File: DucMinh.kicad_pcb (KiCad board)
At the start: 2 copper layers, 80 x 70 mm, 51 parts, among them J5 USB_B_Micro, J8 Conn_01x04, U1 STM32F103C8T6, U2 AMS1117-3.3, U3 LM2596SX-5.0/NOPB, U4 TMC2209_SILENTSTEPSTICK, Y1 8 MHz, Y3 32.768 kHz

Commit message: fix routes
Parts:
- C11: value 10uF -> 10uf; footprint Capacitor_SMD:C_1206_3216Metric_Pad1.33x1.80mm_HandSolder -> ul_tantalum6032:tue_tantalum_6032
- R2: footprint Capacitor_SMD:C_0603_1608Metric_Pad1.08x0.95mm_HandSolder -> Resistor_SMD:R_0603_1608Metric_Pad0.98x0.95mm_HandSolder
- moved C11 6.54 mm to (102.1, 104.3), turned to 0 degrees
- moved R11 5.80 mm to (113.0, 94.8)
- moved R14 5.80 mm to (113.0, 93.2)
- moved R15 5.80 mm to (113.0, 91.5)
- moved PWR1 5.13 mm to (96.5, 110.1)
- moved R3 5.13 mm to (96.5, 113.6), turned to 0 degrees
- moved U2 3.46 mm to (96.5, 104.8)
- moved C19 1.87 mm to (109.1, 96.7)
- moved R2 1.75 mm to (96.5, 111.9)
- renumbered PWR to PWR1, SW to SW1, TMC_EN to TMC_EN1
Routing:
- net VIN_LDO: track 12.7 -> 0.00 mm
- net +3V3: track 224.5 -> 234.5 mm
- net USB-: track 10.4 -> 15.6 mm
- net USB+: track 11.2 -> 15.8 mm
- net GND: track 43.5 -> 39.1 mm, vias 42 -> 44
- net RESET: track 45.7 -> 47.9 mm
- net Net-(J5-D+): track 16.4 -> 14.4 mm
- net Net-(J5-D-): track 16.5 -> 14.9 mm

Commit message: .
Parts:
- removed BOOT1: BOOT1, ul_switch-SS12D00:tue_SS12D00_3P_2.5mm
- removed C15, C16: 10pf, Capacitor_SMD:C_0603_1608Metric_Pad1.08x0.95mm_HandSolder
- removed Y3: 32.768 kHz, ul_crytsal_mc306:SOJ_MC-306_EPS
- added STLink_EN: POWER, Connector_PinHeader_2.54mm:PinHeader_1x02_P2.54mm_Vertical, F.Cu at (125.7, 117.9)
- SWD1: value SWD -> Conn_01x04; footprint Connector_PinHeader_2.54mm:PinHeader_1x03_P2.54mm_Vertical -> Connector_JST:JST_XH_B4B-XH-A_1x04_P2.50mm_Vertical
- moved R7 12.7 mm to (117.8, 105.7), turned to -45 degrees
- moved C14 9.78 mm to (140.3, 122.7), turned to 0 degrees
- moved R8 9.04 mm to (112.2, 125.1), turned to 180 degrees
- moved BOOT0 7.03 mm to (110.0, 129.4)
- moved Y1 5.70 mm to (136.1, 126.4)
- moved SWD1 5.38 mm to (125.7, 126.8)
- moved R4 3.43 mm to (130.9, 110.9), turned to 135 degrees
- moved R5 2.17 mm to (134.9, 89.5)
- moved TMC_EN 2.17 mm to (133.0, 89.4)
- moved PC13 1.98 mm to (130.0, 114.0)
- moved C13 0.81 mm to (136.9, 122.7), turned to 180 degrees
- moved C7 0.81 mm to (134.9, 108.7)
- moved FB1 0.81 mm to (138.5, 108.5)
- moved C8 0.81 mm to (136.1, 109.8)
- moved C6 0.76 mm to (133.7, 107.5)
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- renumbered PWR1 to PWR, TMC_EN1 to TMC_EN
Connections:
- PWM1 pad 1-3: unconnected-(PWM1-Pad1-3) -> 5V_Drive
- PWM1 pad 2-3: unconnected-(PWM1-Pad2-3) -> 5V_Drive
- PWM1 pad 3-3: unconnected-(PWM1-Pad3-3) -> 5V_Drive
- R7 pad 1: BOOT1 -> GND
- SWD1 pad 1: GND -> 3V3_STLINK
- U1 pad 3: LSE_OCS_IN -> unconnected-(U1A-PC14-OSC32_IN-Pad3)
- U1 pad 4: LSE_OCS_OUT -> unconnected-(U1A-PC15-OSC32_OUT-Pad4)
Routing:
- net +3V3: track 234.5 -> 156.7 mm, vias 6 -> 4
- net LSE_OCS_OUT: track 22.9 -> 0.00 mm
- net LSE_OCS_IN: track 15.0 -> 0.00 mm
- net Net-(U1A-PB2): track 26.2 -> 13.3 mm
- net GND: track 39.1 -> 27.3 mm, vias 44 -> 46
- net SWD_CLK: track 17.2 -> 27.3 mm
- net Net-(U1A-BOOT0): track 15.2 -> 22.9 mm, vias 2 -> 4
- net HSE_OCS_OUT: track 31.0 -> 23.3 mm
- net SWD_IO: track 23.7 -> 31.2 mm
- net BOOT1: track 7.03 -> 0.00 mm
- net 3V3_STLINK: track 0.00 -> 6.31 mm
- net 5V_Drive: track 0.00 -> 5.08 mm
- net BOOT0: track 7.02 -> 3.17 mm
- net PC13_LED: track 5.61 -> 2.24 mm
- net HSE_OCS_IN: track 21.1 -> 22.4 mm
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- added copper zone on F.Cu, net (none)
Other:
- board text added: "5V"
- board text added: "CLK"
- board text added: "Default: Jumper OFF"
- board text added: "IO"
- board text removed: "SWD"
- board text removed: "clk"
- board text removed: "gnd"
- board text removed: "io"

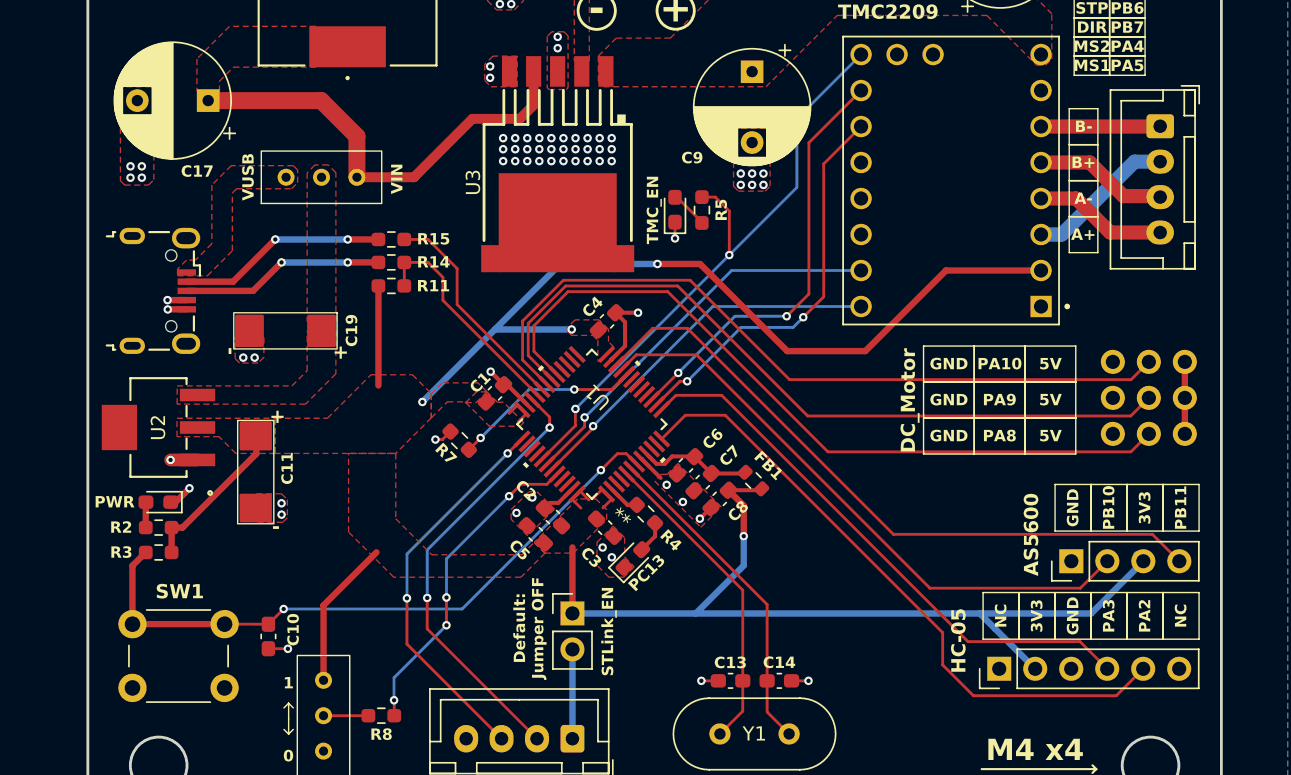
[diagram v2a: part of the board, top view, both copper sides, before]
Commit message: add 74hct125 routes
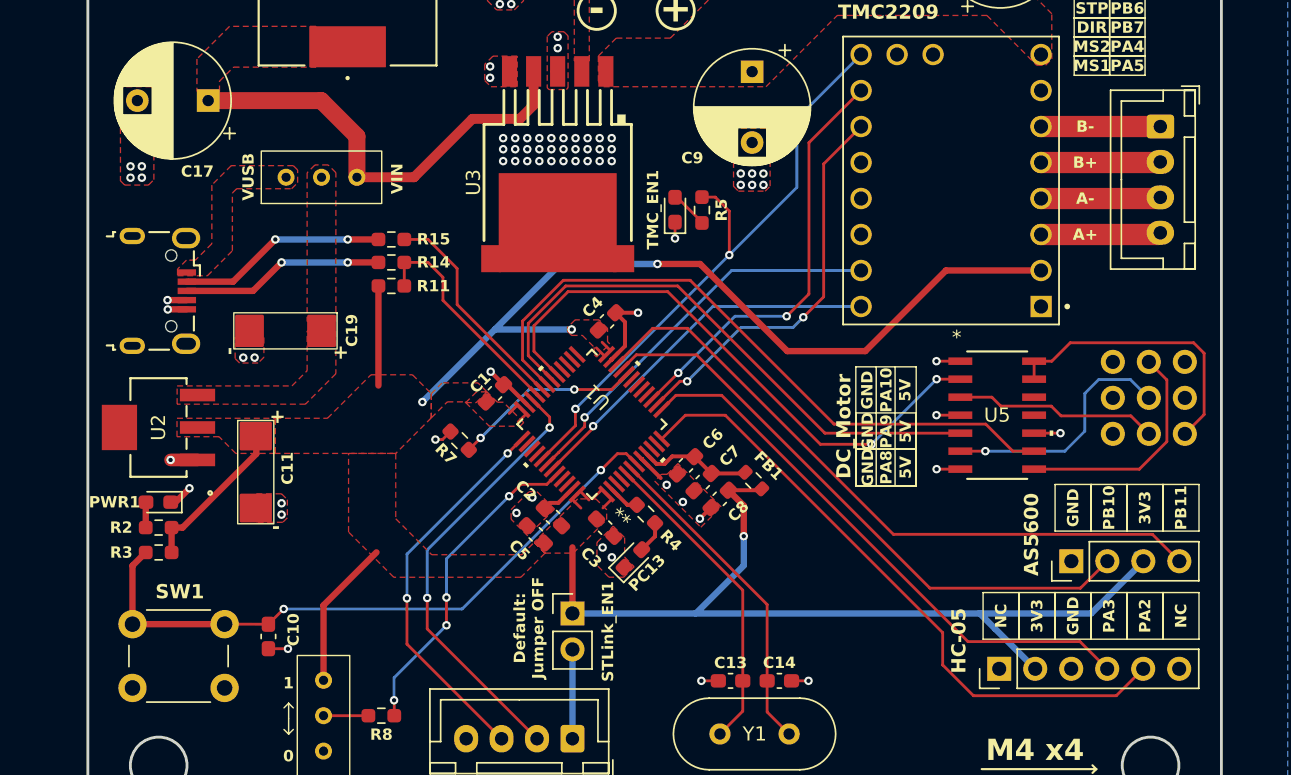
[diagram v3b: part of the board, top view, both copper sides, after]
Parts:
- added U5: 74HCT125D, tue_74hct125:SOT108-1_NXP, F.Cu at (155.7, 103.9)
- C18: value 100nf -> 470uf
- renumbered PWR to PWR1, STLink_EN to STLink_EN1, TMC_EN to TMC_EN1
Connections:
- J8 pad 2: Motor_B+ -> Motor_A-
- J8 pad 3: Motor_A- -> Motor_A+
- J8 pad 4: Motor_A+ -> Motor_B+
- PWM1 pad 1-2: PWM1 -> PWM1_out
- PWM1 pad 1-3: 5V_Drive -> 5V_Drive1
- PWM1 pad 2-2: PWM2 -> PWM2_out
- PWM1 pad 2-3: 5V_Drive -> 5V_Drive2
- PWM1 pad 3-2: PWM3 -> PWM3_out
- PWM1 pad 3-3: 5V_Drive -> 5V_Drive3
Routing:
- net 5V_Drive1: track 0.00 -> 20.4 mm
- net PWM2_out: track 0.00 -> 17.5 mm, vias 0 -> 1
- net PWM3_out: track 0.00 -> 16.3 mm
- net PWM1_out: track 0.00 -> 14.4 mm
- net PWM2: track 54.0 -> 40.6 mm
- net PWM1: track 53.7 -> 41.6 mm, vias 0 -> 2
- net GND: track 27.3 -> 34.2 mm, vias 46 -> 50
- net PWM3: track 54.0 -> 47.5 mm
- net 5V_Drive: track 5.08 -> 0.00 mm
- net Motor_B+: track 10.5 -> 8.47 mm
- net +3V3: track 156.7 -> 158.3 mm
- net Motor_A-: track 9.42 -> 8.44 mm
- net Motor_A+: track 9.40 -> 8.51 mm
- removed copper zone on F.Cu, net (none)

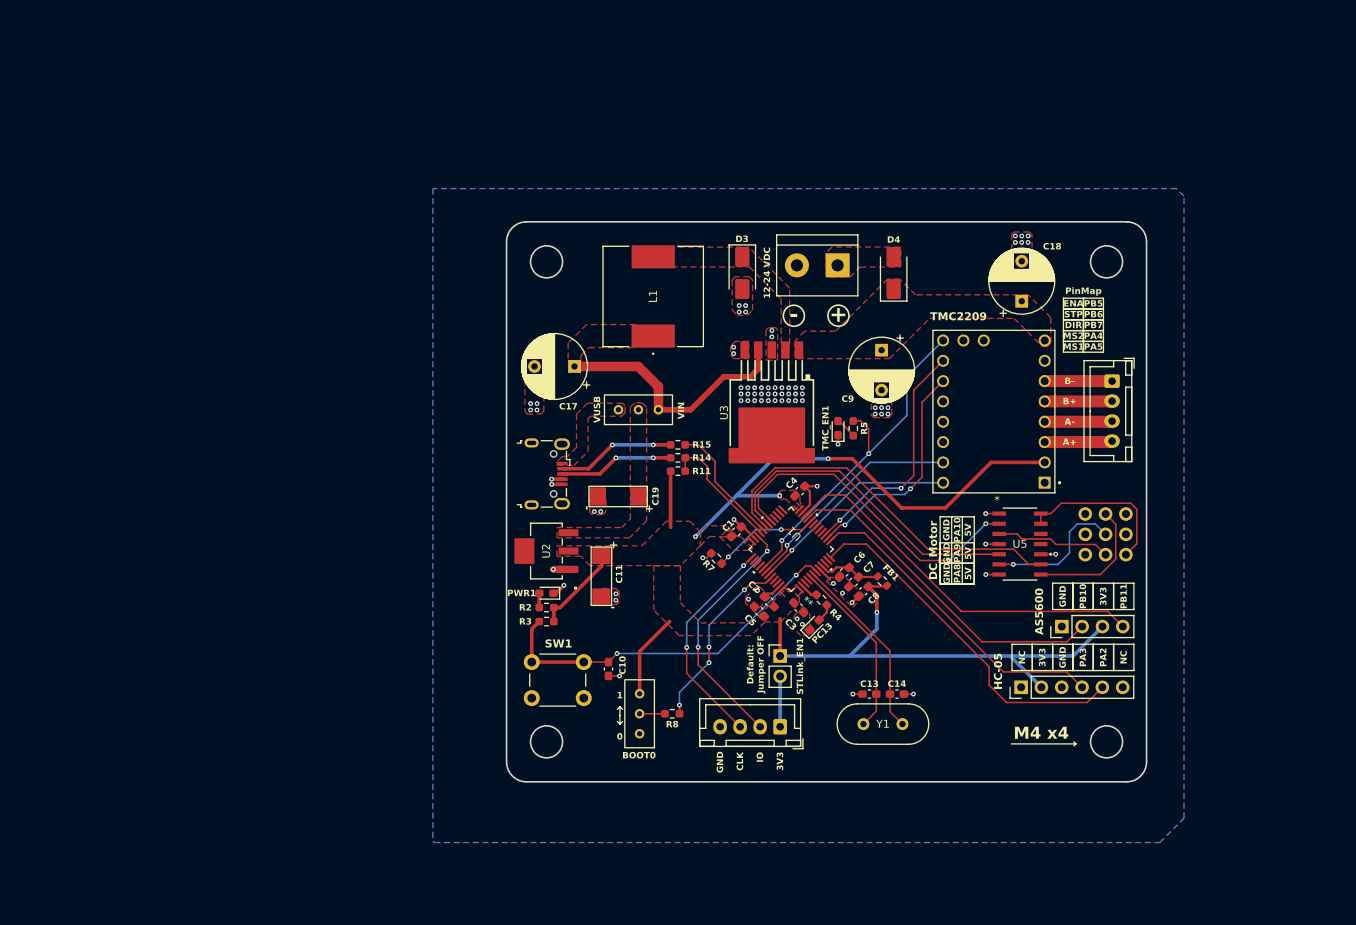
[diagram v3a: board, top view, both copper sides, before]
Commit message: add bts7960
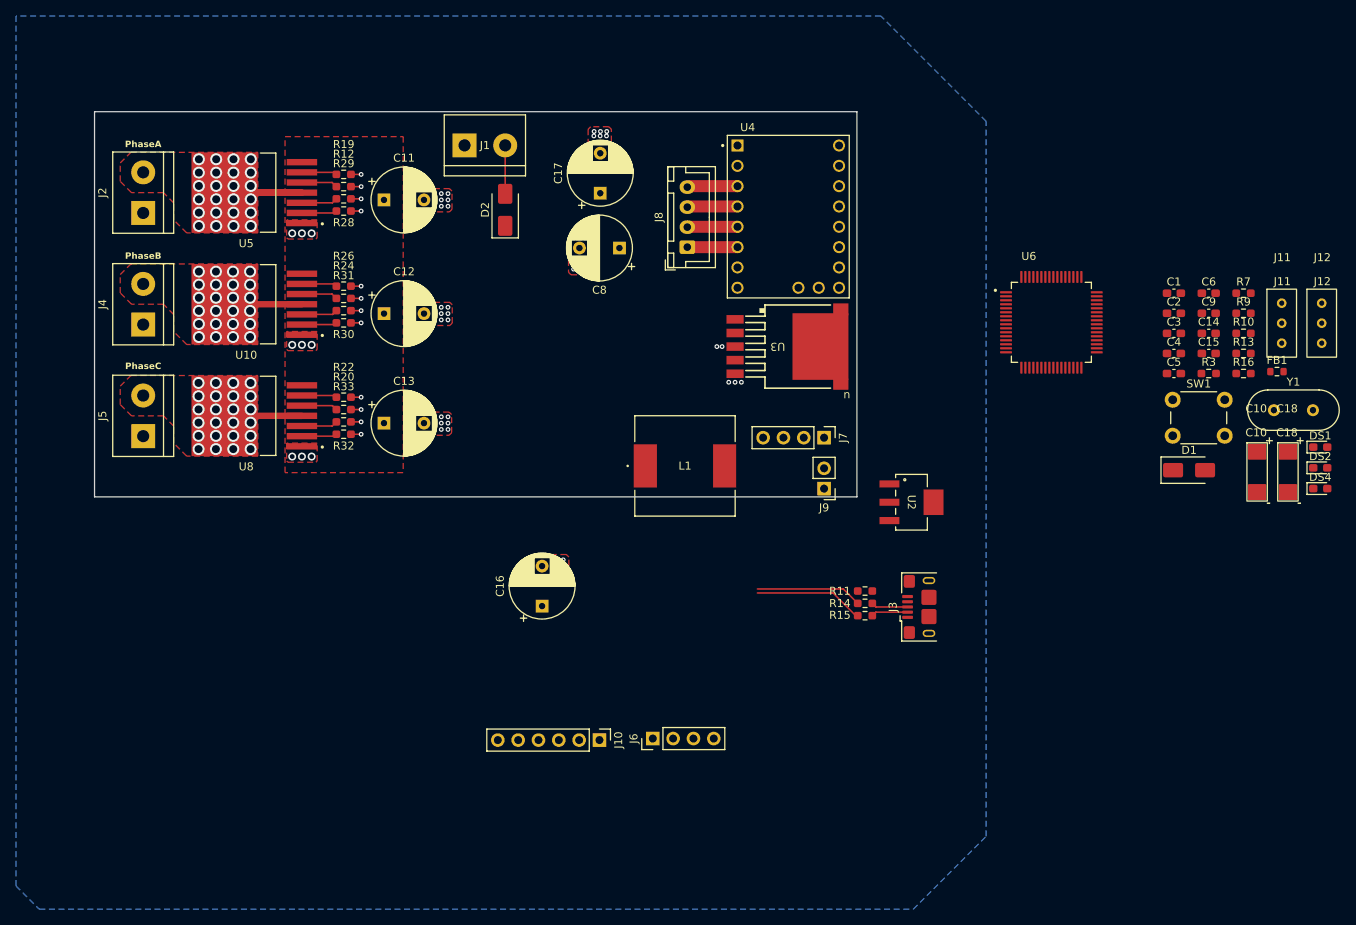
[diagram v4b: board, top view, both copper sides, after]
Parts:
- removed AS5600: AS5600, Connector_PinHeader_2.54mm:PinHeader_1x04_P2.54mm_Vertical
- removed BOOT0: BOOT0, ul_switch-SS12D00:tue_SS12D00_3P_2.5mm
- removed C19: 10uf, ul_tantalum6032:tue_tantalum_6032
- removed C7: 1uf, Capacitor_SMD:C_0603_1608Metric_Pad1.08x0.95mm_HandSolder
- removed D3, D4: SS34, Diode_SMD:D_SMA
- removed HC05: HC05, Connector_PinHeader_2.54mm:PinHeader_1x06_P2.54mm_Vertical
- removed PC13, PWR1, TMC_EN1: LED, LED_SMD:LED_0603_1608Metric_Pad1.05x0.95mm_HandSolder
- removed POWER1: POWER, ul_TerminalBlock:TerminalBlock_bornier-2_P5.08mm
- removed PWM1: ~, ul_Conn_03x03:tue_conn_03x03_2.54mm
- removed R2, R4, R5: 1k, Resistor_SMD:R_0603_1608Metric_Pad0.98x0.95mm_HandSolder
- removed R8: 10k, Resistor_SMD:R_0603_1608Metric_Pad0.98x0.95mm_HandSolder
- removed STLink_EN1: POWER, Connector_PinHeader_2.54mm:PinHeader_1x02_P2.54mm_Vertical
- removed SWD1: Conn_01x04, Connector_JST:JST_XH_B4B-XH-A_1x04_P2.50mm_Vertical
- removed U1: STM32F103C8T6, ul_stm32:LQFP48_STM
- removed VIN1: Conn_01x03, ul_switch-SS12D00:tue_SS12D00_3P_2.5mm
- added C12: 330uf, Capacitor_THT:CP_Radial_D8.0mm_P5.00mm, F.Cu at (76.2, 75.1)
- added C15: 20pf, Capacitor_SMD:C_0603_1608Metric_Pad1.08x0.95mm_HandSolder, F.Cu at (179.3, 80.1)
- added C16: 330uF, Capacitor_THT:CP_Radial_D8.0mm_P5.00mm, F.Cu at (96.0, 111.7)
- added D1: SS34, Diode_SMD:D_SMA, F.Cu at (176.8, 94.7)
- added D2: SS34, Diode_SMD:D_SMA, F.Cu at (91.4, 62.2)
- added DS1: LED_PWR, LED_SMD:LED_0603_1608Metric_Pad1.05x0.95mm_HandSolder, F.Cu at (193.2, 91.8)
- added DS2: LED_PC13, LED_SMD:LED_0603_1608Metric_Pad1.05x0.95mm_HandSolder, F.Cu at (193.2, 94.4)
- added DS4: LED_TMC_EN, LED_SMD:LED_0603_1608Metric_Pad1.05x0.95mm_HandSolder, F.Cu at (193.2, 97.0)
- added J1: Power, tue_TerminalBlock:TerminalBlock_bornier-2_P5.08mm, F.Cu at (86.3, 54.1)
- added J10: HC05, Connector_PinHeader_2.54mm:PinHeader_1x06_P2.54mm_Vertical, F.Cu at (103.1, 128.4)
- added J11: PWR_Selection, tue_switch-SS12D00:tue_SS12D00_3P_2.5mm, F.Cu at (186.6, 72.1)
- added J12: BOOT0, tue_switch-SS12D00:tue_SS12D00_3P_2.5mm, F.Cu at (191.6, 72.1)
- added J2: M1, tue_TerminalBlock:TerminalBlock_bornier-2_P5.08mm, F.Cu at (46.1, 62.5)
- added J3: USB_B_Micro, Connector_USB:USB_Micro-B_Amphenol_10118193-0001LF_Horizontal, F.Cu at (144.3, 111.8)
- added J4: M2, tue_TerminalBlock:TerminalBlock_bornier-2_P5.08mm, F.Cu at (46.1, 76.5)
- added J6: AS5600, Connector_PinHeader_2.54mm:PinHeader_1x04_P2.54mm_Vertical, F.Cu at (109.8, 128.2)
- added J7: STLink, Connector_PinHeader_2.54mm:PinHeader_1x04_P2.54mm_Vertical, F.Cu at (131.2, 90.6)
- added J9: STLink_EN, Connector_PinHeader_2.54mm:PinHeader_1x02_P2.54mm_Vertical, F.Cu at (131.2, 97.0)
- added R10: 10k, Resistor_SMD:R_0603_1608Metric_Pad0.98x0.95mm_HandSolder, F.Cu at (183.7, 77.6)
- added R12: 10k, Resistor_SMD:R_0603_1608Metric_Pad0.98x0.95mm_HandSolder, F.Cu at (71.2, 59.2)
- added R13: 1k, Resistor_SMD:R_0603_1608Metric_Pad0.98x0.95mm_HandSolder, F.Cu at (183.7, 80.1)
- added R16: 1k, Resistor_SMD:R_0603_1608Metric_Pad0.98x0.95mm_HandSolder, F.Cu at (183.7, 82.6)
- added R19: 10k, Resistor_SMD:R_0603_1608Metric_Pad0.98x0.95mm_HandSolder, F.Cu at (71.2, 57.7)
- added R20: 10k, Resistor_SMD:R_0603_1608Metric_Pad0.98x0.95mm_HandSolder, F.Cu at (71.2, 87.1)
- added R22: 10k, Resistor_SMD:R_0603_1608Metric_Pad0.98x0.95mm_HandSolder, F.Cu at (71.2, 85.6)
- added R24: 10k, Resistor_SMD:R_0603_1608Metric_Pad0.98x0.95mm_HandSolder, F.Cu at (71.2, 73.2)
- added R26: 10k, Resistor_SMD:R_0603_1608Metric_Pad0.98x0.95mm_HandSolder, F.Cu at (71.2, 71.7)
- added R28: 10k, Resistor_SMD:R_0603_1608Metric_Pad0.98x0.95mm_HandSolder, F.Cu at (71.2, 62.3)
- added R29: 10k, Resistor_SMD:R_0603_1608Metric_Pad0.98x0.95mm_HandSolder, F.Cu at (71.2, 60.8)
- added R30: 10k, Resistor_SMD:R_0603_1608Metric_Pad0.98x0.95mm_HandSolder, F.Cu at (71.2, 76.3)
- added R31: 10k, Resistor_SMD:R_0603_1608Metric_Pad0.98x0.95mm_HandSolder, F.Cu at (71.2, 74.8)
- added R32: 10k, Resistor_SMD:R_0603_1608Metric_Pad0.98x0.95mm_HandSolder, F.Cu at (71.2, 90.2)
- added R33: 10k, Resistor_SMD:R_0603_1608Metric_Pad0.98x0.95mm_HandSolder, F.Cu at (71.2, 88.7)
- added R9: 10k, Resistor_SMD:R_0603_1608Metric_Pad0.98x0.95mm_HandSolder, F.Cu at (183.7, 75.1)
- added U10: BTS7960B, tue_bts7960b:DPAK127P1490X440-8N, F.Cu at (60.0, 74.0)
- added U6: STM32F103RCT6, tue_stm32f103rct6:QFP50P1200X1200X160-64N, F.Cu at (159.6, 76.2)
- added U8: BTS7960B, tue_bts7960b:DPAK127P1490X440-8N, F.Cu at (60.0, 87.9)
- C10: value 100nf -> 10uf; footprint Capacitor_SMD:C_0603_1608Metric_Pad1.08x0.95mm_HandSolder -> tue_tantalum6032:tue_tantalum_6032
- C11: value 10uf -> 330uf; footprint ul_tantalum6032:tue_tantalum_6032 -> Capacitor_THT:CP_Radial_D8.0mm_P5.00mm
- C13: value 20pf -> 330uf; footprint Capacitor_SMD:C_0603_1608Metric_Pad1.08x0.95mm_HandSolder -> Capacitor_THT:CP_Radial_D8.0mm_P5.00mm
- C17: value 330uF -> 470uf
- C18: value 470uf -> 10uf; footprint Capacitor_THT:CP_Radial_D8.0mm_P5.00mm -> tue_tantalum6032:tue_tantalum_6032
- C5: value 10uf -> 100nf
- C6: value 100nf -> 1uf
- C8: value 1uf -> 330uF; footprint Capacitor_SMD:C_0603_1608Metric_Pad1.08x0.95mm_HandSolder -> Capacitor_THT:CP_Radial_D8.0mm_P5.00mm
- C9: value 330uF -> 100nf; footprint Capacitor_THT:CP_Radial_D8.0mm_P5.00mm -> Capacitor_SMD:C_0603_1608Metric_Pad1.08x0.95mm_HandSolder
- J5: value USB_B_Micro -> M3; footprint ul_USB:USB_Micro-B_Wuerth-629105150521 -> tue_TerminalBlock:TerminalBlock_bornier-2_P5.08mm
- J8: value Conn_01x04 -> Stepper_Motor
- L1: footprint ul_inductor_smd:tue__CDRH127LDNP-470MC_SUM -> tue_inductor_smd:tue__CDRH127LDNP-470MC_SUM
- R7: value 10k -> 1k
- U2: footprint ul_ams1117:SOT_AMS_ADS -> tue_ams1117:SOT_AMS_ADS
- U3: footprint ul_lm2596hvs:tue_lm2596 -> tue_lm2596hvs:tue_lm2596
- U4: footprint ul_TMC2209:tue_TMC2209 -> tue_TMC2209:tue_TMC2209
- U5: value 74HCT125D -> BTS7960B; footprint tue_74hct125:SOT108-1_NXP -> tue_bts7960b:DPAK127P1490X440-8N
- moved U5 105.3 mm to (60.0, 60.0), turned to 180 degrees
- moved R3 88.4 mm to (179.3, 82.6)
- moved SW1 86.6 mm to (174.8, 85.9)
- moved C10 84.7 mm to (184.1, 91.3), turned to 0 degrees
- moved R7 73.8 mm to (183.7, 72.6), turned to 0 degrees
- moved C13 69.5 mm to (76.2, 88.8), turned to 0 degrees
- moved Y1 64.6 mm to (187.4, 87.2)
- moved C1 62.3 mm to (174.9, 72.6), turned to 0 degrees
- moved C2 62.1 mm to (174.9, 75.1), turned to 0 degrees
- moved C5 59.7 mm to (174.9, 82.6), turned to 0 degrees
- moved C14 59.6 mm to (179.3, 77.6)
- moved C3 58.1 mm to (174.9, 77.6), turned to 0 degrees
- moved C6 57.4 mm to (179.3, 72.6), turned to 0 degrees
- moved FB1 55.8 mm to (187.8, 82.4), turned to 0 degrees
- moved J8 55.7 mm to (114.1, 66.8), turned to 90 degrees
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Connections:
- C10 pad 1: RESET -> +3V3
- C11 pad 1: +3V3 -> VDC
- C13 pad 1: HSE_OCS_IN -> VDC
- C14 pad 1: HSE_OCS_OUT -> Net-(U6-PD1_OSC_OUT)
- C17 pad 1: 5V_LDO -> VDC
- C18 pad 1: VDC -> VIN_LDO
- C6 pad 1: Net-(U1B-VDDA) -> +3V3
- C8 pad 1: +3V3 -> VDC
- C9 pad 1: VDC -> RESET
- FB1 pad 1: Net-(U1B-VDDA) -> /VDDA
- J5 pad 1: 5V_USB -> GND
- J5 pad 2: Net-(J5-D-) -> M3+
- R14 pad 1: Net-(J5-D+) -> Net-(J3-D+)
- R15 pad 1: Net-(J5-D-) -> Net-(J3-D-)
- R7 pad 1: GND -> Net-(DS1-A)
- R7 pad 2: Net-(U1A-PB2) -> +3V3
- U5 pad 2: PWM1 -> Net-(U5-IN)
- U5 pad 3: PWM1_out -> Net-(U5-INH)
- U5 pad 4: GND -> M1+
- U5 pad 5: PWM2 -> Net-(U5-SR)
- U5 pad 6: PWM2_out -> Net-(U5-IS)
- U5 pad 7: GND -> VDC
- U5 pad 8: PWM3_out -> M1+
- Y1 pad 1: HSE_OCS_IN -> Net-(U6-PD1_OSC_OUT)
- Y1 pad 2: HSE_OCS_OUT -> Net-(U6-PD0-OSC_IN)
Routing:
- net +3V3: track 158.3 -> 0.00 mm, vias 4 -> 0
- net RESET: track 47.9 -> 0.00 mm, vias 2 -> 0
- net SDA2: track 46.8 -> 0.00 mm
- net PWM3: track 47.5 -> 1.27 mm, vias 0 -> 1
- net TX2: track 45.1 -> 0.00 mm
- net ENABLE_PIN: track 43.3 -> 0.00 mm, vias 2 -> 0
- net SCL2: track 42.3 -> 0.00 mm
- net PWM1: track 41.6 -> 1.27 mm, vias 2 -> 1
- net RX2: track 39.7 -> 0.00 mm
- net PWM2: track 40.6 -> 1.27 mm, vias 0 -> 1
- net 5V_LDO: track 31.9 -> 0.00 mm
- net SWD_IO: track 31.2 -> 0.00 mm, vias 2 -> 0
- net MS1_PIN: track 30.1 -> 0.00 mm, vias 2 -> 0
- net STEP_PIN: track 28.2 -> 0.00 mm, vias 1 -> 0
- net MS2_PIN: track 28.0 -> 0.00 mm, vias 2 -> 0
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- added copper zone on F.Cu, net M1+
- added copper zone on F.Cu, net M2+
- added copper zone on F.Cu, net M3+
- removed copper zone on F.Cu, net +3V3
- removed copper zone on F.Cu, net 5V_LDO
- removed copper zone on F.Cu, net 5V_USB
- removed copper zone on F.Cu, net Net-(D1-K)
- removed copper zone on F.Cu, net Net-(D4-A)
- removed copper zone on F.Cu, net VIN_LDO
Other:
- board size 80 x 70 mm -> 95.3 x 48.1 mm
- board text added: "PhaseA"
- board text added: "PhaseB"
- board text added: "PhaseC"
- board text removed: "+"
- board text removed: "-"
- board text removed: "0"
- board text removed: "1"
- board text removed: "12-24 VDC"
- board text removed: "3V3"
- board text removed: "5V"
- board text removed: "A+"
- board text removed: "A-"
- board text removed: "AS5600"
- board text removed: "B+"
- board text removed: "B-"
- board text removed: "CLK"
- board text removed: "DC_Motor"
- board text removed: "DIR"
- board text removed: "Default: Jumper OFF"
- board text removed: "ENA"
- board text removed: "GND"
- board text removed: "HC-05"
- board text removed: "IO"
- board text removed: "M4 x4"
- board text removed: "MS1"
- board text removed: "MS2"
- board text removed: "NC"
- board text removed: "PA10"
- board text removed: "PA2"
- board text removed: "PA3"
- board text removed: "PA4"
- board text removed: "PA5"
- board text removed: "PA8"
- board text removed: "PA9"
- board text removed: "PB10"
- board text removed: "PB11"
- board text removed: "PB5"
- board text removed: "PB6"
- board text removed: "PB7"
- board text removed: "PinMap"
- board text removed: "STP"
- board text removed: "TMC2209"
- board text removed: "VIN"
- board text removed: "VUSB"
